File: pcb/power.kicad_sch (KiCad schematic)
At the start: 39 parts, among them U3 TPS63802DLAR, U4 BQ24078RGTR, U6 SN74LVC1G79DBVT

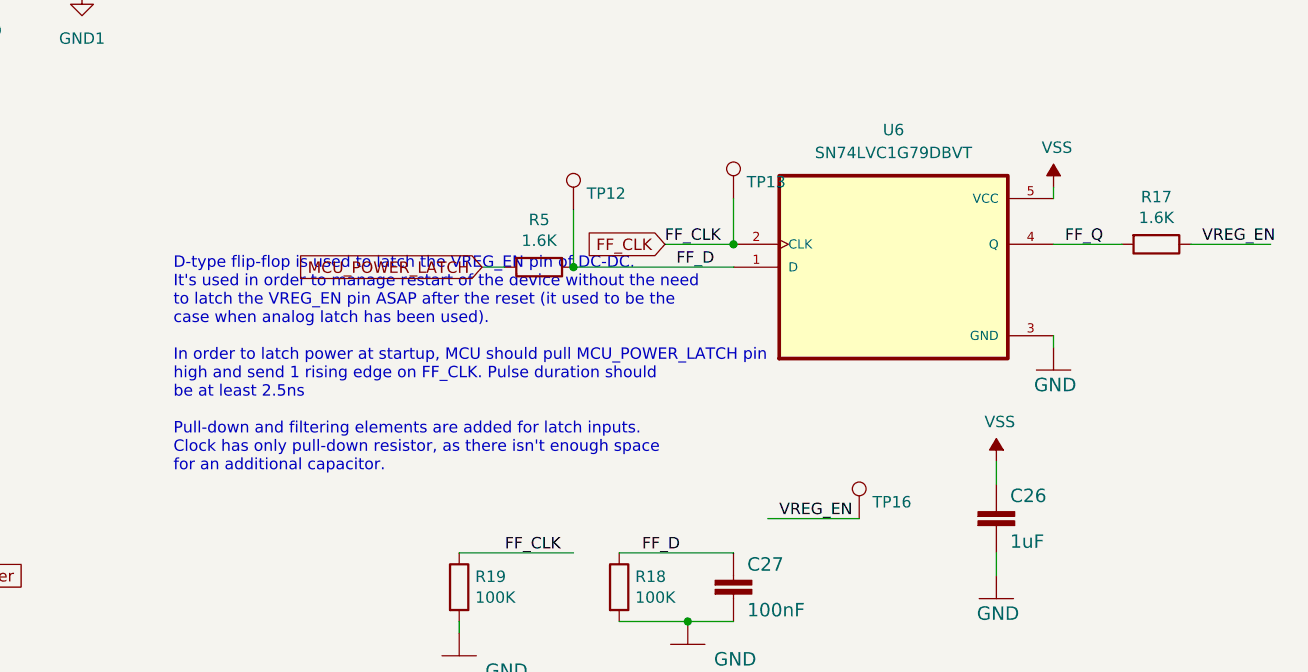
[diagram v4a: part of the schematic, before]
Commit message: [pcb] finalized main work on fixture 1.3
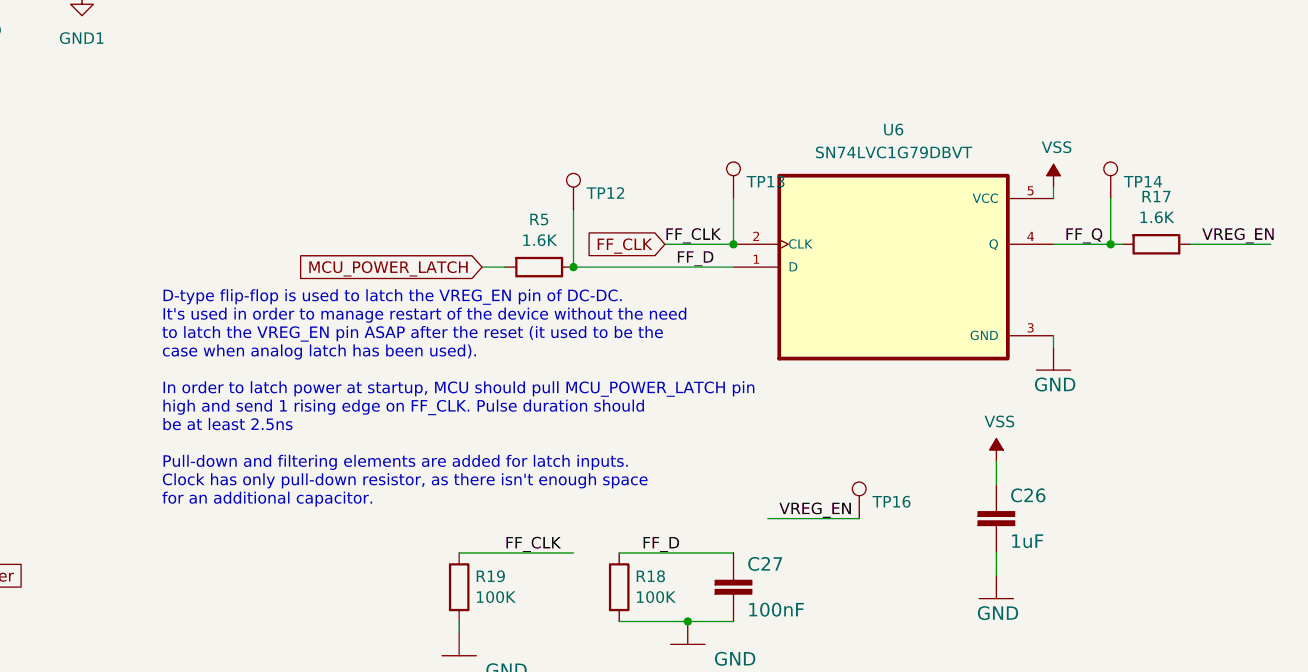
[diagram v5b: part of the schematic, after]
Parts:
- added TP14: TestPoint, TestPoint:TestPoint_Pad_D1.0mm, symbol Connector:TestPoint
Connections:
- net FF_Q: now also TP14.1
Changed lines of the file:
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@@
 (kicad_sch (version 20211123) (generator eeschema)
   (paper "A4")
+  (junction (at 276.86 120.65) (diameter 0) (color 0 0 0 0)
+  )
   (junction (at 207.01 73.66) (diameter 0) (color 0 0 0 0)
   )
@@
     (stroke (width 0) (type default) (color 0 0 0 0))
   )
+  (wire (pts (xy 276.86 115.57) (xy 276.86 120.65))
+    (stroke (width 0) (type default) (color 0 0 0 0))
+  )
   (wire (pts (xy 138.43 163.83) (xy 138.43 170.18))
     (stroke (width 0) (type default) (color 0 0 0 0))
@@
     (stroke (width 0) (type default) (color 0 0 0 0))
   )
+  (wire (pts (xy 276.86 120.65) (xy 278.13 120.65))
+    (stroke (width 0) (type default) (color 0 0 0 0))
+  )
   (wire (pts (xy 217.17 73.66) (xy 217.17 74.93))
     (stroke (width 0) (type default) (color 0 0 0 0))
@@
     (stroke (width 0) (type default) (color 0 0 0 0))
   )
-  (wire (pts (xy 270.51 120.65) (xy 278.13 120.65))
+  (wire (pts (xy 270.51 120.65) (xy 276.86 120.65))
     (stroke (width 0) (type default) (color 0 0 0 0))
   )
@@
   )
   (text "D-type flip-flop is used to latch the VREG_EN pin of DC-DC.\nIt's used in order to manage restart of the device without the need \nto latch the VREG_EN pin ASAP after the reset (it used to be the \ncase when analog latch has been used).\n\nIn order to latch power at startup, MCU should pull MCU_POWER_LATCH pin\nhigh and send 1 rising edge on FF_CLK. Pulse duration should \nbe at least 2.5ns\n\nPull-down and filtering elements are added for latch inputs.\nClock has only pull-down resistor, as there isn't enough space \nfor an additional capacitor."
-    (at 172.72 146.05 0)
+    (at 171.45 149.86 0)
     (effects (font (size 1.27 1.27)) (justify left bottom))
   )
@@
       (effects (font (size 1.27 1.27)) hide)
     )
+    (pin "1")
+  )
+  (symbol (lib_id "Connector:TestPoint") (at 276.86 115.57 0) (unit 1)
+    (in_bom yes) (on_board yes)
+    (property "Reference" "TP14" (id 0) (at 278.3332 113.7412 0)
+      (effects (font (size 1.27 1.27)) (justify left))
+    )
+    (property "Value" "TestPoint" (id 1) (at 278.3332 114.8842 0)
+      (effects (font (size 1.27 1.27)) (justify left) hide)
+    )
+    (property "Footprint" "TestPoint:TestPoint_Pad_D1.0mm" (id 2) (at 281.94 115.57 0)
+      (effects (font (size 1.27 1.27)) hide)
+    )
+    (property "Datasheet" "~" (id 3) (at 281.94 115.57 0)
+      (effects (font (size 1.27 1.27)) hide)
+    )

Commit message: [pcb] added missing LCSC IDs to Dictofun 1.3
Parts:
- C1, C2: LCSC (none) -> C109447
- L1: LCSC (none) -> C1333867
- R14: LCSC (none) -> C25741
- R15: LCSC (none) -> C144750
- R16: LCSC (none) -> C4190
- U3: LCSC (none) -> C2845237
- U6: LCSC (none) -> C42878
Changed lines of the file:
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@@
       (effects (font (size 1.27 1.27)) hide)
     )
-    (property "LCSC" "" (id 4) (at 162.56 71.12 0)
+    (property "LCSC" "C144750" (id 4) (at 162.56 71.12 0)
       (effects (font (size 1.27 1.27)) hide)
     )
@@
     (property "MANUFACTURER" "Texas Instruments" (id 7) (at 134.62 77.47 0)
       (effects (font (size 1.27 1.27)) (justify left bottom) hide)
+    )
+    (property "LCSC" "C2845237" (id 8) (at 134.62 77.47 0)
+      (effects (font (size 1.27 1.27)) hide)
     )
     (pin "1")
@@
       (effects (font (size 1.27 1.27)) hide)
     )
-    (property "LCSC" "" (id 4) (at 207.01 77.47 0)
+    (property "LCSC" "C109447" (id 4) (at 207.01 77.47 0)
       (effects (font (size 1.27 1.27)) hide)
     )
@@
       (effects (font (size 1.27 1.27)) hide)
     )
+    (property "LCSC" "C1333867" (id 5) (at 111.76 86.36 0)
+      (effects (font (size 1.27 1.27)) hide)
+    )
     (pin "1")
     (pin "2")
@@
       (effects (font (size 1.27 1.27)) hide)
     )
-    (property "LCSC" "" (id 4) (at 162.56 83.82 0)
+    (property "LCSC" "C4190" (id 4) (at 162.56 83.82 0)
       (effects (font (size 1.27 1.27)) hide)
     )
@@
       (effects (font (size 1.27 1.27)) hide)
     )
-    (property "LCSC" "" (id 4) (at 186.69 77.47 0)
+    (property "LCSC" "C109447" (id 4) (at 186.69 77.47 0)
       (effects (font (size 1.27 1.27)) hide)
     )
@@
       (effects (font (size 1.27 1.27)) (justify left bottom) hide)
     )
+    (property "LCSC" "C42878" (id 4) (at 252.73 123.19 0)
+      (effects (font (size 1.27 1.27)) hide)
+    )
     (pin "1")
     (pin "2")
@@
       (effects (font (size 1.27 1.27)) hide)
     )
-    (property "LCSC" "" (id 4) (at 175.26 73.66 0)
-      (effects (font (size 1.27 1.27)) hide)
-    )
+    (property "LCSC" "C25741" (id 4) (at 175.26 73.66 0)
+      (effects (font (size 1.27 1.27)) hide)
+    )

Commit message: start laying out 1.4
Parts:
- added J4: Conn_01x02_Socket, _other:SM02B-SRSS-TB_LF__SN_, symbol Connector:Conn_01x02_Socket
- added J5: Conn_01x03_Socket, _other:JST_SM03B-SRSS-TB_LF__SN_, symbol Connector:Conn_01x03_Socket
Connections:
- net +BATT: now also J4.2 (Pin_2)
- net GND: now also J4.1 (Pin_1), J5.1 (Pin_1)
- new net DBG_RX: J5.3 (Pin_3)
- new net DBG_TX: J5.2 (Pin_2)
